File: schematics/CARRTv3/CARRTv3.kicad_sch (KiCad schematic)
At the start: 31 parts, among them J1 LCD_with_5_Buttons, M1 Rear Right, M2 Front Right, M3 Front Left, M4 Rear Left, M5 Lidar Servo, P1 PowerBoost_1000C, SW1 Switch, SW2 RPi0 Shutdown, SW3 Right Encoder, SW4 Left Encoder, SW5 Switch, T1 2N2222, U1 BNO055, X1 Raspberry_Pi_Zero2, X2 Raspberry_Pico2

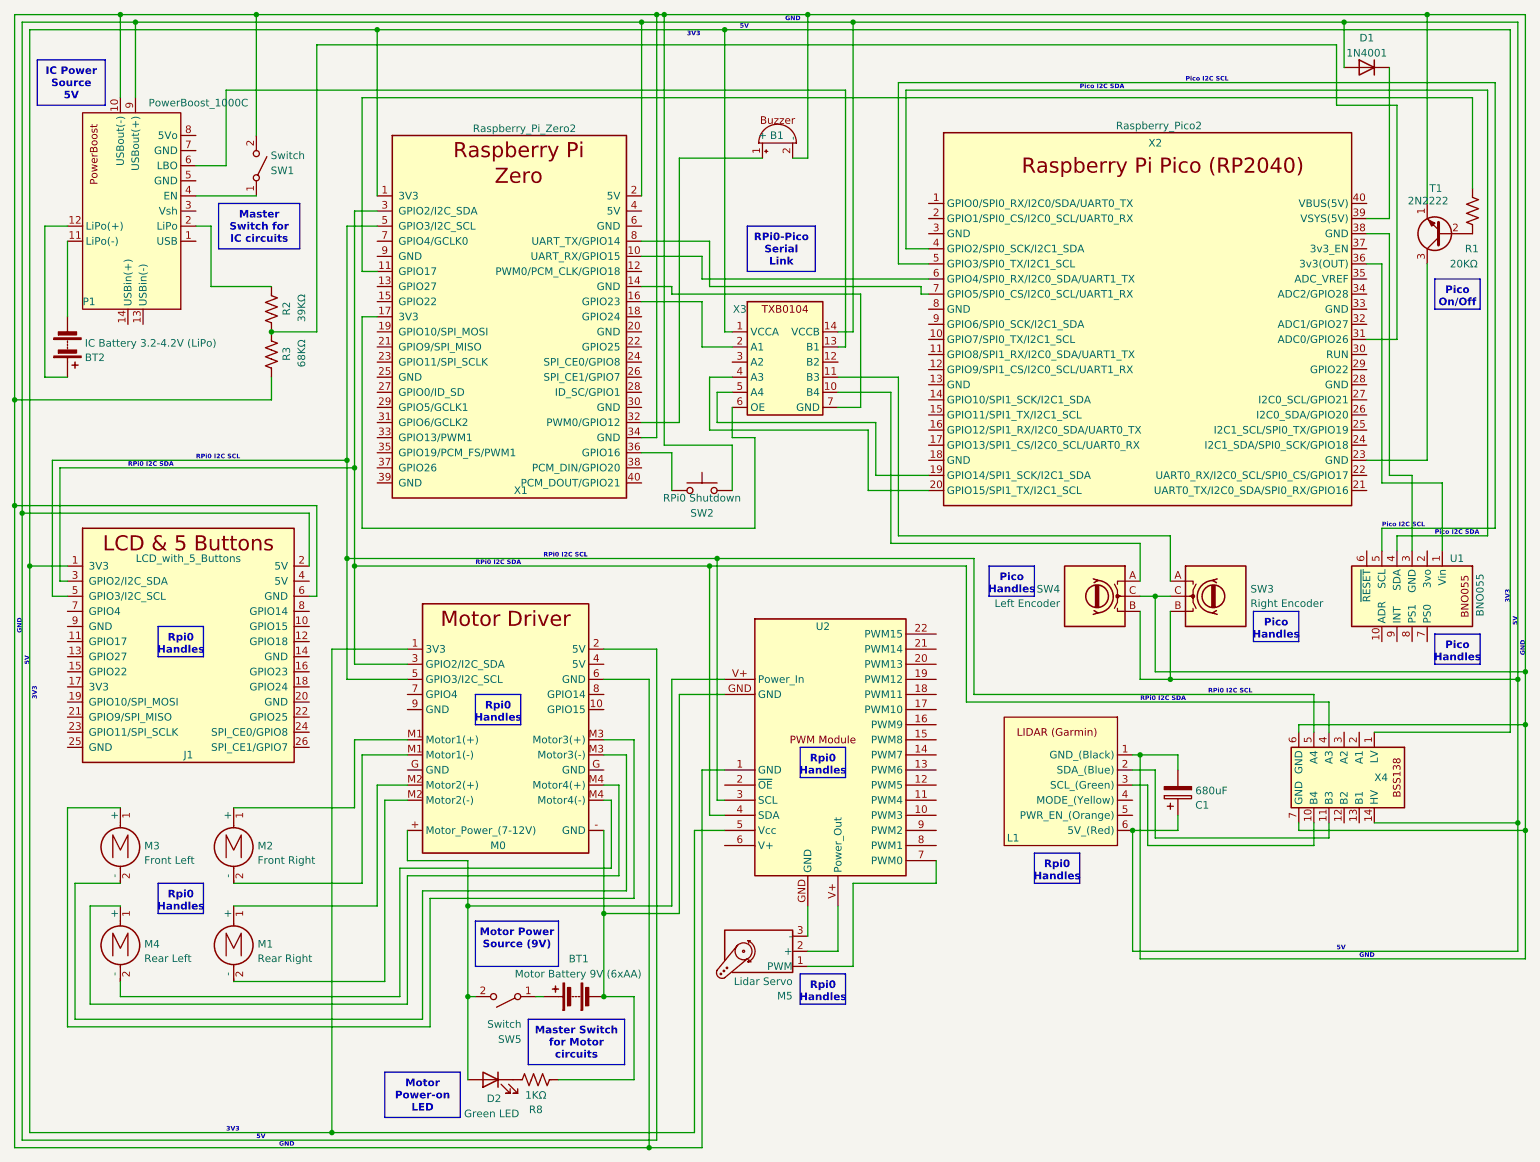
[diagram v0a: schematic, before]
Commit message: Update schematics for UBEC, etc
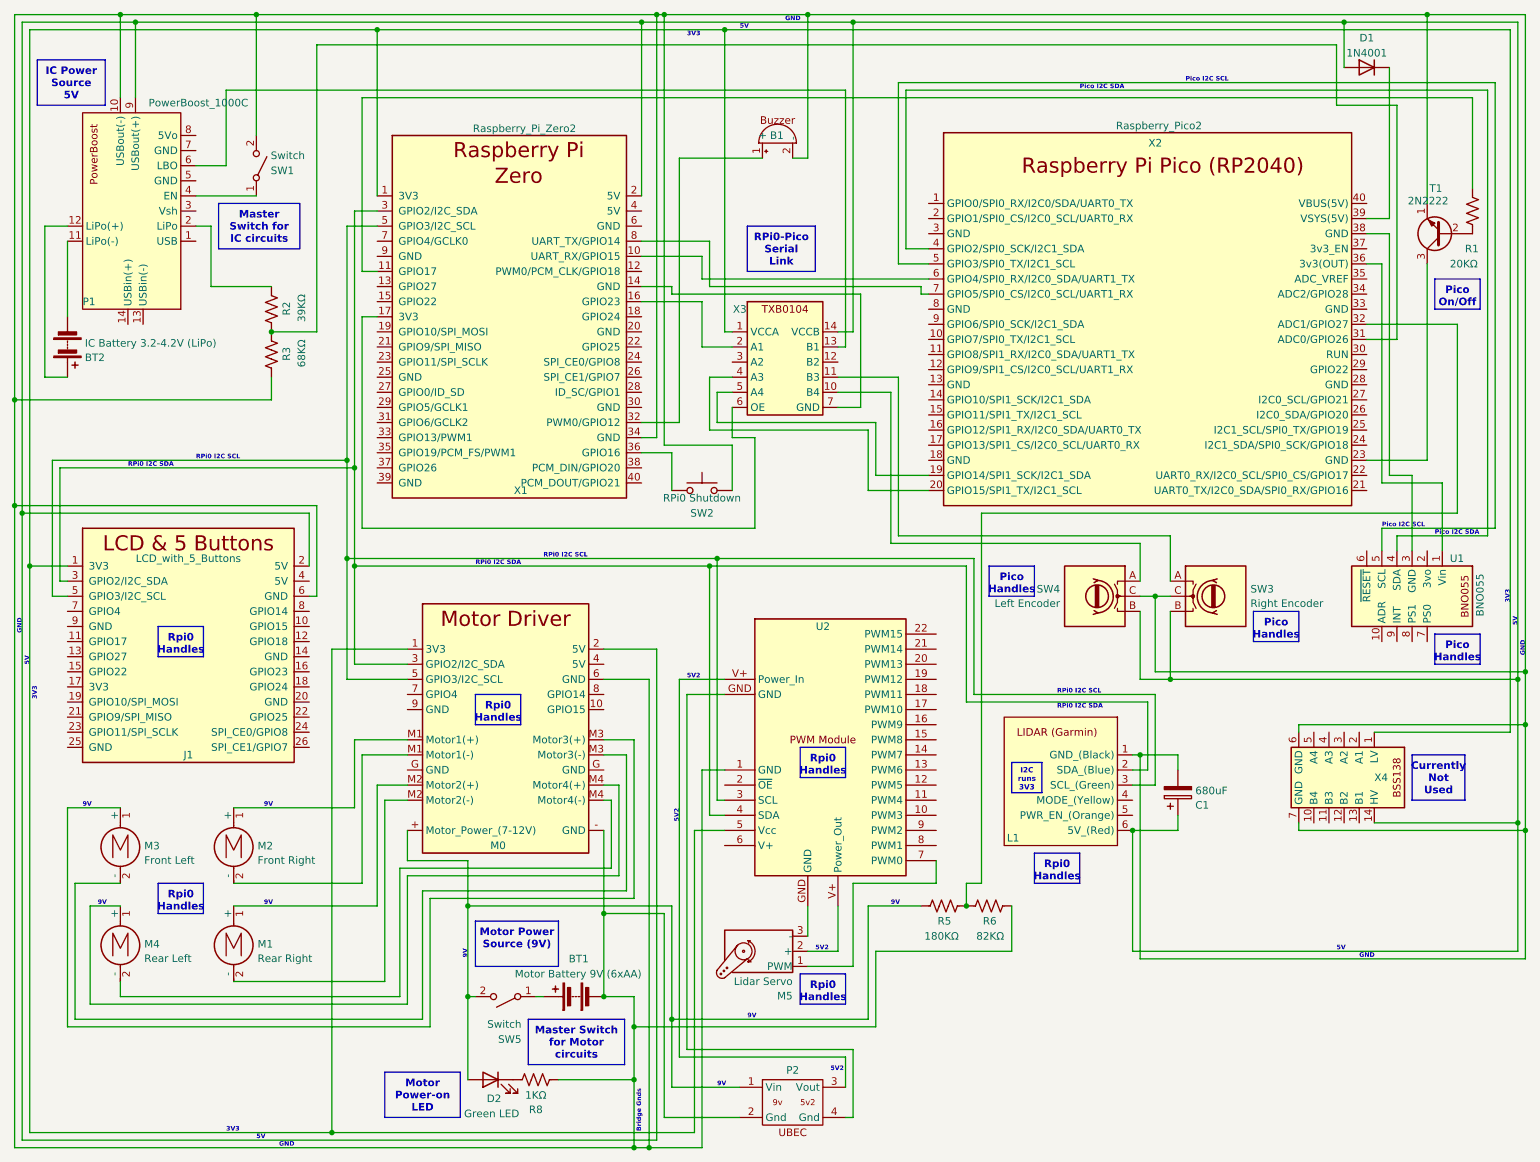
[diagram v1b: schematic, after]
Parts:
- added P2: ~, symbol CARRTv3:UBEC
- added R5: 180KΩ, symbol Device:R_US
- added R6: 82KΩ, symbol Device:R_US
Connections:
- net at B1.2 (-), C1.2, J1.6 (GND)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: now also BT1.2 (-), M0.- (GND), R8.2, P2.2 (Gnd), R6.2
- net at X4.10 (B4): no longer L1.3 (SCL_(Green))
- net at X4.11 (B3): no longer L1.2 (SDA_(Blue))
- net at J1.3 (GPIO2/I2C_SDA), M0.3 (GPIO2/I2C_SDA), U2.4 (SDA)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: now also L1.2 (SDA_(Blue)); no longer X4.4 (A3)
- net at J1.5 (GPIO3/I2C_SCL), M0.5 (GPIO3/I2C_SCL), U2.3 (SCL)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: now also L1.3 (SCL_(Green)); no longer X4.5 (A4)
- net at D2.2 (A), M0.+ (Motor_Power_(7-12V)), SW5.2 (B): now also P2.1 (Vin), R5.1; no longer U2.V+ (Power_Out)
- net at X2.32 (ADC1/GPIO27): now also R5.2, R6.1
- new net: P2.4 (Gnd), U2.GND
- new net: P2.3 (Vout), U2.V+ (Power_Out)
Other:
- note added: "5V2"
- note added: "9V"
- note added: "Bridge Gnds"

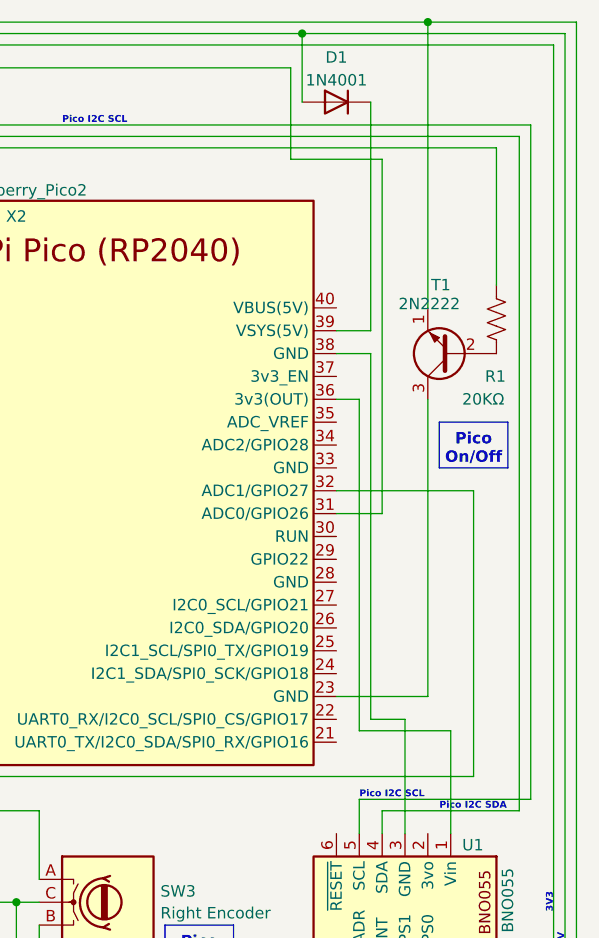
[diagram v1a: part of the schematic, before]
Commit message: Switch ADC0-ADC1 connections; update schematic and connections tables
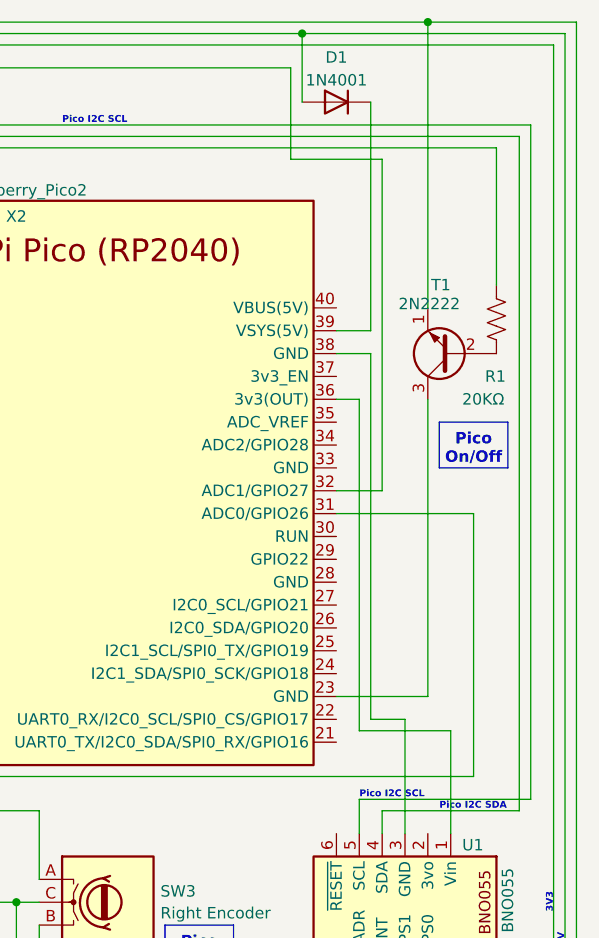
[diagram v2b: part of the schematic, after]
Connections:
- net at R2.1, R3.2: now also X2.32 (ADC1/GPIO27); no longer X2.31 (ADC0/GPIO26)
- net at R5.2, R6.1: now also X2.31 (ADC0/GPIO26); no longer X2.32 (ADC1/GPIO27)
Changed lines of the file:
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@@
     (stroke (width 0) (type default) (color 194 0 0 1))
+  )
+  (wire (pts (xy 240.03 64.77) (xy 245.11 64.77))
+    (stroke (width 0) (type default))
   )
   (wire (pts (xy 43.18 43.18) (xy 53.34 43.18))
@@
     (stroke (width 0) (type default))
   )
-  (wire (pts (xy 245.11 67.31) (xy 245.11 27.94))
-    (stroke (width 0) (type default))
-  )
   (wire (pts (xy 15.24 105.41) (xy 15.24 200.66))
     (stroke (width 0) (type default) (color 204 102 0 1))
@@
     (stroke (width 0) (type default) (color 194 0 0 1))
   )
+  (wire (pts (xy 255.27 67.31) (xy 255.27 96.52))
+    (stroke (width 0) (type default))
+  )
   (wire (pts (xy 113.03 144.78) (xy 113.03 156.21))
     (stroke (width 0.2286) (type default) (color 72 0 0 1))
@@
     (stroke (width 0.2286) (type default) (color 132 0 0 1))
   )
+  (wire (pts (xy 245.11 27.94) (xy 245.11 64.77))
+    (stroke (width 0) (type default))
+  )
   (wire (pts (xy 55.88 66.04) (xy 63.5 66.04))
     (stroke (width 0) (type default))
@@
     (stroke (width 0.2286) (type default) (color 132 0 0 1))
   )
+  (wire (pts (xy 240.03 67.31) (xy 255.27 67.31))
+    (stroke (width 0) (type default))
+  )
   (wire (pts (xy 88.9 162.56) (xy 88.9 177.8))
     (stroke (width 0.2286) (type default) (color 132 0 0 1))
@@
     (stroke (width 0) (type default) (color 0 0 132 1))
   )
-  (wire (pts (xy 255.27 64.77) (xy 255.27 96.52))
-    (stroke (width 0) (type default))
-  )
   (wire (pts (xy 143.51 36.83) (xy 146.05 36.83))
     (stroke (width 0) (type default) (color 0 0 0 1))
@@
   (wire (pts (xy 157.48 170.18) (xy 157.48 182.88))
     (stroke (width 0) (type default) (color 0 0 0 1))
-  )
-  (wire (pts (xy 240.03 67.31) (xy 245.11 67.31))
-    (stroke (width 0) (type default))
   )
   (wire (pts (xy 208.28 137.16) (xy 201.93 137.16))
@@
     (stroke (width 0.2286) (type default) (color 72 0 0 1))
   )
-  (wire (pts (xy 240.03 64.77) (xy 255.27 64.77))
-    (stroke (width 0) (type default))
-  )
   (wire (pts (xy 241.3 148.59) (xy 265.43 148.59))

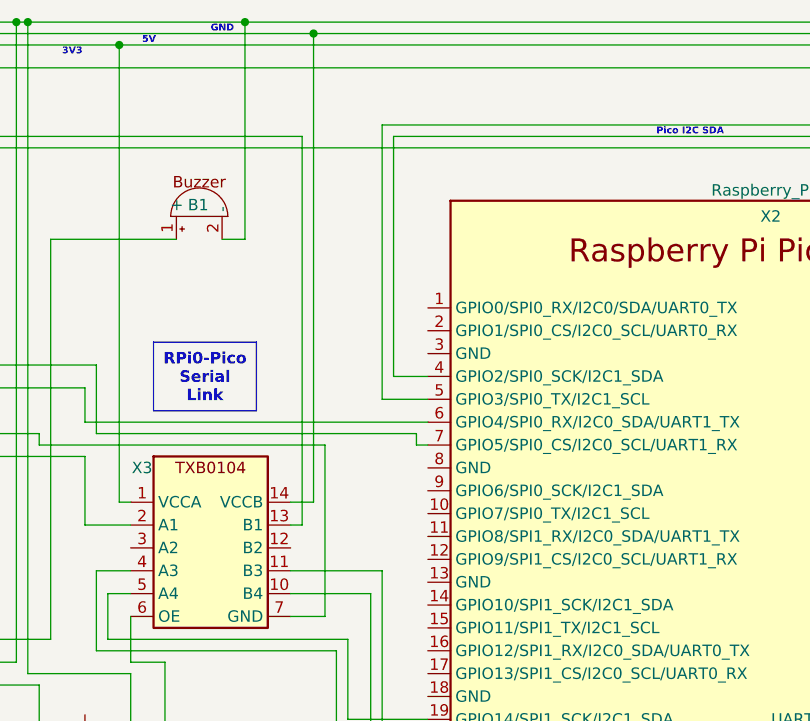
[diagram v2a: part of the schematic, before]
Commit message: Correct I2C connects at Pico
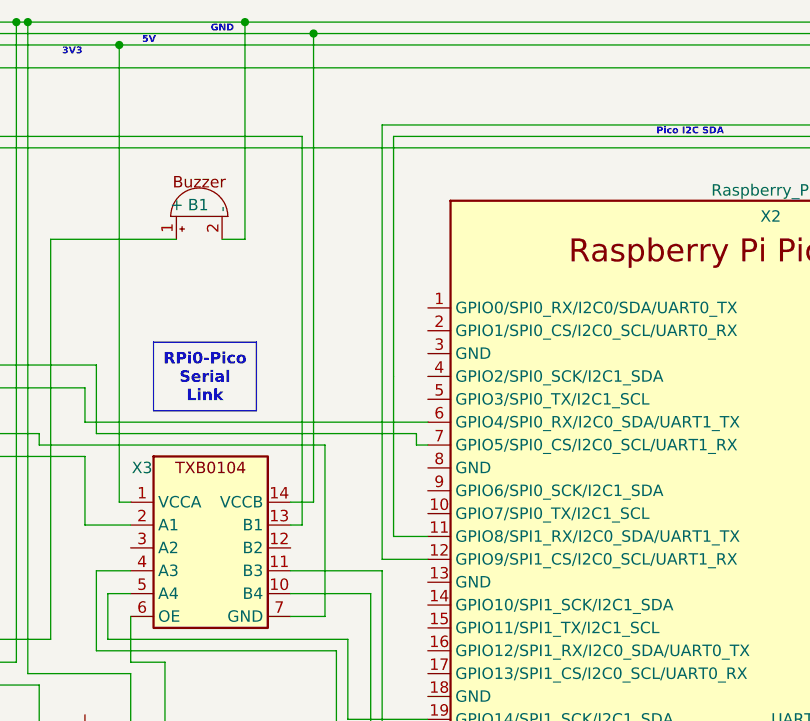
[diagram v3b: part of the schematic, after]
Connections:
- net at X2.11 (GPIO8/SPI1_RX/I2C0_SDA/UART1_TX): now also U1.4 (SDA)
- net at X2.12 (GPIO9/SPI1_CS/I2C0_SCL/UART1_RX): now also U1.5 (SCL)
- net at X2.4 (GPIO2/SPI0_SCK/I2C1_SDA): no longer U1.4 (SDA)
- net at X2.5 (GPIO3/SPI0_TX/I2C1_SCL): no longer U1.5 (SCL)
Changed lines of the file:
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@@
     (stroke (width 0) (type default) (color 204 102 0 1))
+  )
+  (wire (pts (xy 162.56 69.85) (xy 162.56 52.07))
+    (stroke (width 0) (type default))
   )
   (wire (pts (xy 146.05 170.18) (xy 151.13 170.18))
@@
     (stroke (width 0) (type default) (color 132 0 132 1))
   )
-  (wire (pts (xy 166.37 52.07) (xy 162.56 52.07))
-    (stroke (width 0) (type default) (color 0 0 132 1))
-  )
   (wire (pts (xy 118.11 83.82) (xy 120.65 83.82))
     (stroke (width 0) (type default) (color 0 0 0 1))
@@
     (stroke (width 0) (type default) (color 0 72 0 1))
   )
+  (wire (pts (xy 166.37 69.85) (xy 162.56 69.85))
+    (stroke (width 0) (type default))
+  )
   (wire (pts (xy 260.35 100.33) (xy 245.11 100.33))
     (stroke (width 0) (type default) (color 0 0 132 1))
@@
     (stroke (width 0) (type default))
   )
+  (wire (pts (xy 161.29 72.39) (xy 166.37 72.39))
+    (stroke (width 0) (type default) (color 194 194 0 1))
+  )
   (wire (pts (xy 165.1 58.42) (xy 129.54 58.42))
     (stroke (width 0) (type default) (color 132 132 132 1))
@@
     (stroke (width 0) (type default) (color 194 0 0 1))
   )
-  (wire (pts (xy 161.29 54.61) (xy 161.29 24.13))
+  (wire (pts (xy 161.29 24.13) (xy 161.29 72.39))
     (stroke (width 0) (type default) (color 194 194 0 1))
   )
@@
     (stroke (width 0.2286) (type default) (color 132 0 0 1))
   )
-  (wire (pts (xy 166.37 54.61) (xy 161.29 54.61))
-    (stroke (width 0) (type default) (color 194 194 0 1))
-  )
   (wire (pts (xy 234.95 17.78) (xy 234.95 27.94))
